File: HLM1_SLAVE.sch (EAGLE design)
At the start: 7 parts

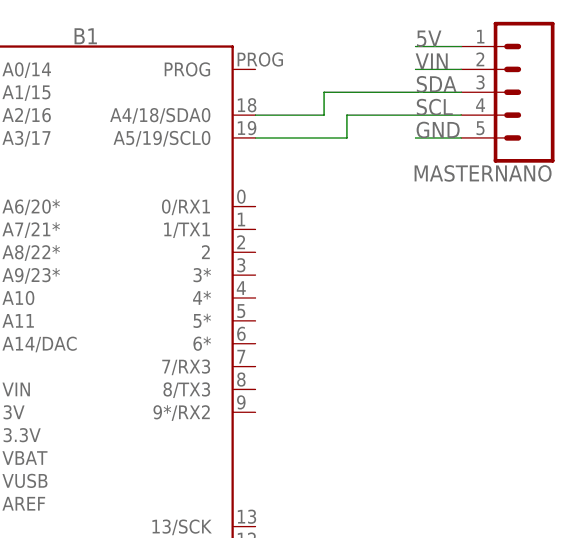
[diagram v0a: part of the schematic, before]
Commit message: Connected I2C lines to slave device for board carving
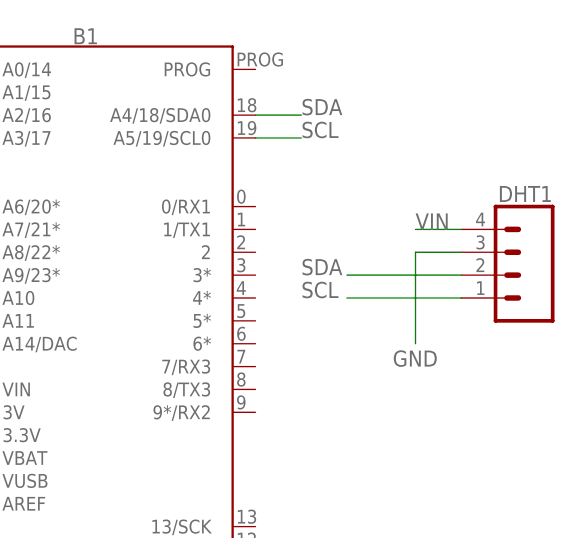
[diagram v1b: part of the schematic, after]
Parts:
- removed MASTERNANO: (no value), SparkFun-Connectors:CONN_05
- added DHT1: (no value), SparkFun-Connectors:CONN_04
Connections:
- removed net 5V: MASTERNANO.1
- net GND: now also DHT1.3; no longer MASTERNANO.5
- net SCL: now also DHT1.1; no longer MASTERNANO.4
- net SDA: now also DHT1.2; no longer MASTERNANO.3
- net VIN: now also DHT1.4; no longer MASTERNANO.2
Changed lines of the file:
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@@
 <?xml version="1.0" encoding="utf-8"?>
 <!DOCTYPE eagle SYSTEM "eagle.dtd">
-<eagle version="8.5.1">
+<eagle version="9.0.1">
 <drawing>
 <settings>
@@
 <part name="TMP36" library="SparkFun-Connectors" deviceset="CONN_03" device=""/>
 <part name="MS5607" library="SparkFun-Connectors" deviceset="CONN_07" device=""/>
-<part name="MASTERNANO" library="SparkFun-Connectors" deviceset="CONN_05" device=""/>
 <part name="TR1" library="discrete" library_urn="urn:adsk.eagle:library:211" deviceset="THERMISTOR_" device="R-5" package3d_urn="urn:adsk.eagle:package:12931/1"/>
 <part name="TR3" library="discrete" library_urn="urn:adsk.eagle:library:211" deviceset="THERMISTOR_" device="R-7,5" package3d_urn="urn:adsk.eagle:package:12930/1"/>
+<part name="DHT1" library="SparkFun-Connectors" deviceset="CONN_04" device=""/>
 </parts>
 <sheets>
@@
 <instance part="TMP36" gate="J$1" x="20.32" y="55.88"/>
 <instance part="MS5607" gate="G$1" x="10.16" y="27.94"/>
-<instance part="MASTERNANO" gate="G$1" x="119.38" y="76.2" rot="R180"/>
 <instance part="TR1" gate="G$1" x="33.02" y="22.86"/>
 <instance part="TR3" gate="G$1" x="33.02" y="33.02"/>
+<instance part="DHT1" gate="G$1" x="116.84" y="55.88" rot="MR0"/>
 </instances>
 <busses>
@@
 <net name="SDA" class="0">
 <segment>
-<pinref part="MASTERNANO" gate="G$1" pin="3"/>
-<label x="106.68" y="76.2" size="1.778" layer="95"/>
-<pinref part="B1" gate="G$1" pin="A4/18/SDA0"/>
-<wire x1="88.9" y1="73.66" x2="96.52" y2="73.66" width="0.1524" layer="91"/>
-<wire x1="96.52" y1="73.66" x2="96.52" y2="76.2" width="0.1524" layer="91"/>
-<wire x1="96.52" y1="76.2" x2="111.76" y2="76.2" width="0.1524" layer="91"/>
-</segment>
-<segment>
 <pinref part="MS5607" gate="G$1" pin="5"/>
 <wire x1="15.24" y1="33.02" x2="22.86" y2="33.02" width="0.1524" layer="91"/>
 <label x="17.78" y="33.02" size="1.778" layer="95"/>
 </segment>
+<segment>
+<pinref part="DHT1" gate="G$1" pin="2"/>
+<wire x1="111.76" y1="55.88" x2="99.06" y2="55.88" width="0.1524" layer="91"/>
+<label x="93.98" y="55.88" size="1.778" layer="95"/>
+</segment>
+<segment>
+<pinref part="B1" gate="G$1" pin="A4/18/SDA0"/>
+<wire x1="88.9" y1="73.66" x2="93.98" y2="73.66" width="0.1524" layer="91"/>
+<label x="93.98" y="73.66" size="1.778" layer="95"/>
+</segment>
 </net>
 <net name="SCL" class="0">
-<segment>
-<pinref part="MASTERNANO" gate="G$1" pin="4"/>
-<label x="106.68" y="73.66" size="1.778" layer="95"/>
-<pinref part="B1" gate="G$1" pin="A5/19/SCL0"/>
-<wire x1="88.9" y1="71.12" x2="99.06" y2="71.12" width="0.1524" layer="91"/>
-<wire x1="99.06" y1="71.12" x2="99.06" y2="73.66" width="0.1524" layer="91"/>
-<wire x1="99.06" y1="73.66" x2="111.76" y2="73.66" width="0.1524" layer="91"/>
-</segment>
 <segment>
 <pinref part="MS5607" gate="G$1" pin="4"/>
@@
 <label x="17.78" y="30.48" size="1.778" layer="95"/>
 </segment>
+<segment>
+<pinref part="DHT1" gate="G$1" pin="1"/>
+<wire x1="111.76" y1="53.34" x2="99.06" y2="53.34" width="0.1524" layer="91"/>
+<label x="93.98" y="53.34" size="1.778" layer="95"/>
+</segment>
+<segment>
+<pinref part="B1" gate="G$1" pin="A5/19/SCL0"/>
+<wire x1="88.9" y1="71.12" x2="93.98" y2="71.12" width="0.1524" layer="91"/>
+<label x="93.98" y="71.12" size="1.778" layer="95"/>
+</segment>
 </net>
 <net name="GND" class="0">
-<segment>
-<pinref part="MASTERNANO" gate="G$1" pin="5"/>
-<wire x1="111.76" y1="71.12" x2="106.68" y2="71.12" width="0.1524" layer="91"/>
-<label x="106.68" y="71.12" size="1.778" layer="95"/>
-</segment>
 <segment>
 <pinref part="DHT22" gate="G$1" pin="1"/>
@@
 <wire x1="43.18" y1="22.86" x2="43.18" y2="20.32" width="0.1524" layer="91"/>
 </segment>
-</net>
-<net name="5V" class="0">
-<segment>
-<pinref part="MASTERNANO" gate="G$1" pin="1"/>
-<wire x1="111.76" y1="81.28" x2="106.68" y2="81.28" width="0.1524" layer="91"/>
-<label x="106.68" y="81.28" size="1.778" layer="95"/>
+<segment>
+<pinref part="DHT1" gate="G$1" pin="3"/>
+<wire x1="111.76" y1="58.42" x2="106.68" y2="58.42" width="0.1524" layer="91"/>
+<wire x1="106.68" y1="58.42" x2="106.68" y2="48.26" width="0.1524" layer="91"/>
+<label x="104.14" y="45.72" size="1.778" layer="95"/>
 </segment>
 </net>
@@
 </segment>
 <segment>
-<pinref part="MASTERNANO" gate="G$1" pin="2"/>
-<wire x1="111.76" y1="78.74" x2="106.68" y2="78.74" width="0.1524" layer="91"/>
-<label x="106.68" y="78.74" size="1.778" layer="95"/>
-</segment>
-</net>
+<pinref part="DHT1" gate="G$1" pin="4"/>
+<wire x1="111.76" y1="60.96" x2="106.68" y2="60.96" width="0.1524" layer="91"/>
+<label x="106.68" y="60.96" size="1.778" layer="95"/>
+</segment>
+</net>

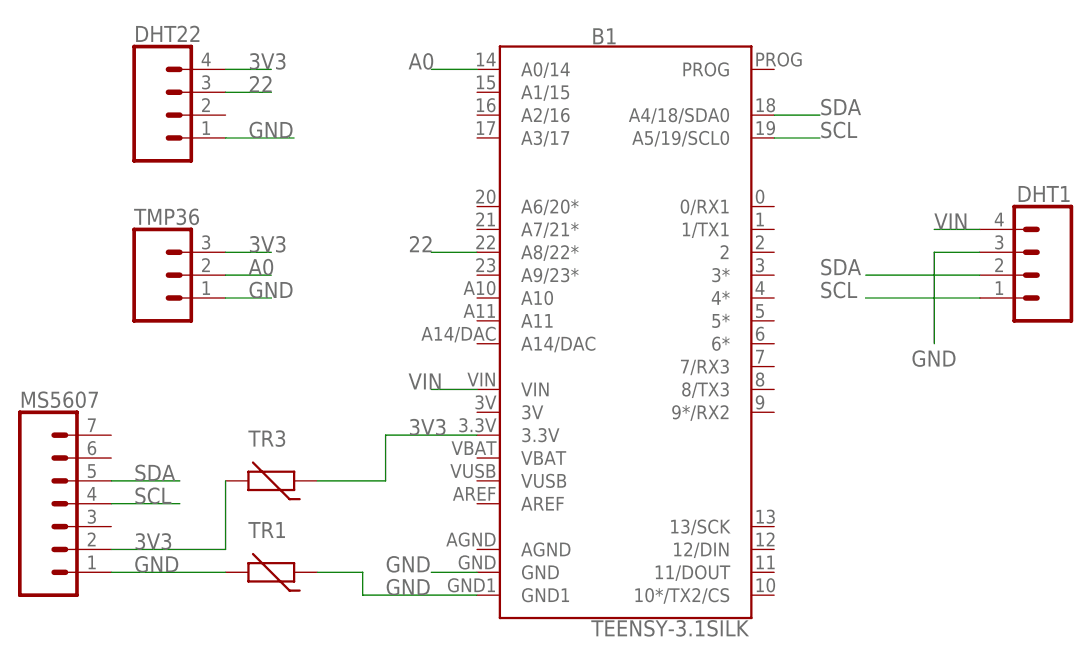
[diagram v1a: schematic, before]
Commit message: Improved routing
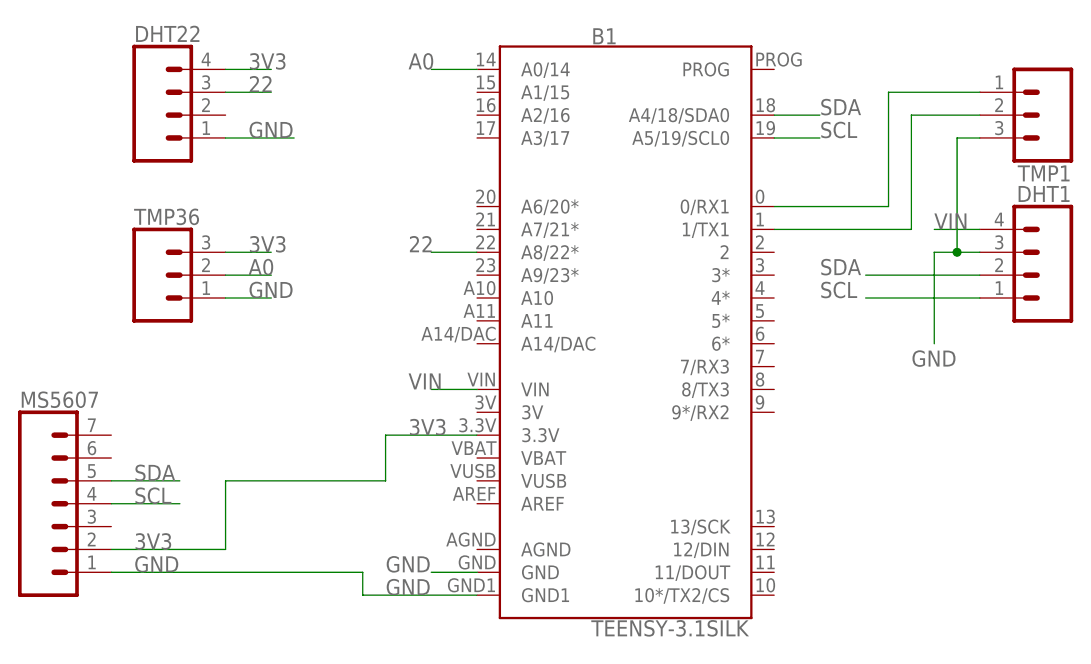
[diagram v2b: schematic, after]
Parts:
- removed TR1: (no value), discrete:THERMISTOR_R-5
- removed TR3: (no value), discrete:THERMISTOR_R-7,5
- added TMP1: (no value), SparkFun-Connectors:CONN_03
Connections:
- new net N$1: B1.0/RX1, TMP1.1
- new net N$2: B1.1/TX1, TMP1.2
- net 3V3: no longer TR3.1, TR3.2
- net GND: now also TMP1.3; no longer TR1.1, TR1.2
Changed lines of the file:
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@@
 <part name="TMP36" library="SparkFun-Connectors" deviceset="CONN_03" device=""/>
 <part name="MS5607" library="SparkFun-Connectors" deviceset="CONN_07" device=""/>
-<part name="TR1" library="discrete" library_urn="urn:adsk.eagle:library:211" deviceset="THERMISTOR_" device="R-5" package3d_urn="urn:adsk.eagle:package:12931/1"/>
-<part name="TR3" library="discrete" library_urn="urn:adsk.eagle:library:211" deviceset="THERMISTOR_" device="R-7,5" package3d_urn="urn:adsk.eagle:package:12930/1"/>
 <part name="DHT1" library="SparkFun-Connectors" deviceset="CONN_04" device=""/>
+<part name="TMP1" library="SparkFun-Connectors" deviceset="CONN_03" device=""/>
 </parts>
 <sheets>
@@
 <instance part="TMP36" gate="J$1" x="20.32" y="55.88"/>
 <instance part="MS5607" gate="G$1" x="10.16" y="27.94"/>
-<instance part="TR1" gate="G$1" x="33.02" y="22.86"/>
-<instance part="TR3" gate="G$1" x="33.02" y="33.02"/>
 <instance part="DHT1" gate="G$1" x="116.84" y="55.88" rot="MR0"/>
+<instance part="TMP1" gate="J$1" x="119.38" y="73.66" rot="R180"/>
 </instances>
 <busses>
@@
 <segment>
 <pinref part="MS5607" gate="G$1" pin="1"/>
-<wire x1="15.24" y1="22.86" x2="27.94" y2="22.86" width="0.1524" layer="91"/>
+<wire x1="15.24" y1="22.86" x2="43.18" y2="22.86" width="0.1524" layer="91"/>
 <label x="17.78" y="22.86" size="1.778" layer="95"/>
-<pinref part="TR1" gate="G$1" pin="2"/>
-</segment>
-<segment>
 <pinref part="B1" gate="G$1" pin="GND1"/>
 <wire x1="55.88" y1="20.32" x2="43.18" y2="20.32" width="0.1524" layer="91"/>
 <label x="45.72" y="20.32" size="1.778" layer="95"/>
-<pinref part="TR1" gate="G$1" pin="1"/>
-<wire x1="38.1" y1="22.86" x2="43.18" y2="22.86" width="0.1524" layer="91"/>
 <wire x1="43.18" y1="22.86" x2="43.18" y2="20.32" width="0.1524" layer="91"/>
 </segment>
 <segment>
 <pinref part="DHT1" gate="G$1" pin="3"/>
-<wire x1="111.76" y1="58.42" x2="106.68" y2="58.42" width="0.1524" layer="91"/>
+<wire x1="111.76" y1="58.42" x2="109.22" y2="58.42" width="0.1524" layer="91"/>
+<wire x1="109.22" y1="58.42" x2="106.68" y2="58.42" width="0.1524" layer="91"/>
 <wire x1="106.68" y1="58.42" x2="106.68" y2="48.26" width="0.1524" layer="91"/>
 <label x="104.14" y="45.72" size="1.778" layer="95"/>
+<wire x1="109.22" y1="58.42" x2="109.22" y2="71.12" width="0.1524" layer="91"/>
+<junction x="109.22" y="58.42"/>
+<pinref part="TMP1" gate="J$1" pin="3"/>
+<wire x1="109.22" y1="71.12" x2="111.76" y2="71.12" width="0.1524" layer="91"/>
 </segment>
 </net>
@@
 <net name="3V3" class="0">
 <segment>
-<pinref part="B1" gate="G$1" pin="3.3V"/>
-<wire x1="55.88" y1="38.1" x2="45.72" y2="38.1" width="0.1524" layer="91"/>
-<label x="48.26" y="38.1" size="1.778" layer="95"/>
-<wire x1="38.1" y1="33.02" x2="45.72" y2="33.02" width="0.1524" layer="91"/>
-<wire x1="45.72" y1="33.02" x2="45.72" y2="38.1" width="0.1524" layer="91"/>
-<pinref part="TR3" gate="G$1" pin="1"/>
-</segment>
-<segment>
 <pinref part="TMP36" gate="J$1" pin="3"/>
 <wire x1="27.94" y1="58.42" x2="33.02" y2="58.42" width="0.1524" layer="91"/>
@@
 <label x="17.78" y="25.4" size="1.778" layer="95"/>
 <wire x1="27.94" y1="25.4" x2="27.94" y2="33.02" width="0.1524" layer="91"/>
-<pinref part="TR3" gate="G$1" pin="2"/>
+<pinref part="B1" gate="G$1" pin="3.3V"/>
+<wire x1="55.88" y1="38.1" x2="45.72" y2="38.1" width="0.1524" layer="91"/>
+<label x="48.26" y="38.1" size="1.778" layer="95"/>
+<wire x1="45.72" y1="33.02" x2="45.72" y2="38.1" width="0.1524" layer="91"/>
+<wire x1="27.94" y1="33.02" x2="45.72" y2="33.02" width="0.1524" layer="91"/>
 </segment>
 </net>
@@
 </segment>
 </net>
+<net name="N$1" class="0">
+<segment>
+<pinref part="B1" gate="G$1" pin="0/RX1"/>
+<wire x1="88.9" y1="63.5" x2="101.6" y2="63.5" width="0.1524" layer="91"/>
+<wire x1="101.6" y1="63.5" x2="101.6" y2="76.2" width="0.1524" layer="91"/>
+<pinref part="TMP1" gate="J$1" pin="1"/>
+<wire x1="101.6" y1="76.2" x2="111.76" y2="76.2" width="0.1524" layer="91"/>
+</segment>
+</net>
+<net name="N$2" class="0">
+<segment>
+<pinref part="B1" gate="G$1" pin="1/TX1"/>
+<wire x1="88.9" y1="60.96" x2="104.14" y2="60.96" width="0.1524" layer="91"/>
+<wire x1="104.14" y1="60.96" x2="104.14" y2="73.66" width="0.1524" layer="91"/>
+<pinref part="TMP1" gate="J$1" pin="2"/>
+<wire x1="104.14" y1="73.66" x2="111.76" y2="73.66" width="0.1524" layer="91"/>
+</segment>
+</net>
 </nets>
 </sheet>
@@
 </schematic>
 </drawing>
-<compatibility>
-<note version="8.2" severity="warning">
-Since Version 8.2, EAGLE supports online libraries. The ids
-of those online libraries will not be understood (or retained)
-with this version.
-</note>
-<note version="8.3" severity="warning">
-Since Version 8.3, EAGLE supports URNs for individual library
-assets (packages, symbols, and devices). The URNs of those assets
-will not be understood (or retained) with this version.
-</note>
-<note version="8.3" severity="warning">
-Since Version 8.3, EAGLE supports the association of 3D packages
-with devices in libraries, schematics, and board files. Those 3D
-packages will not be understood (or retained) with this version.
-</note>
-</compatibility>
 </eagle>
